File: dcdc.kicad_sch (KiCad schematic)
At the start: 25 parts, among them U2 LMR51450F

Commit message: Start layout
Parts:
- removed TP12: SW, meteopress_footprints:TestPoint_THTPad_D2.0mm_Drill1.0mm, symbol Connector:TestPoint
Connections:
- net V_{out}: now also R23.1
- net SW: now reaches C7.2, L1.1, U2.1 (SW), U2.2 (SW), U2.3 (SW)
- net SW: no longer R23.1
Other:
- moved on the sheet: JP2, L1, R23, R24

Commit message: Minor updates
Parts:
- removed C13, C14, C15, C16, C17, C18, C19: 10u, Capacitor_SMD:C_1206_3216Metric, symbol Device:C
- added C6: 100u (EEEFTH101XAP), Capacitor_SMD:CP_Elec_6.3x7.7, symbol Device:C_Polarized
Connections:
- net GND: now also C6.2
- net V_{out}: now also C6.1
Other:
- moved on the sheet: C10, C11, C12, C20, C7, C8, C9, D1, JP2, L1, R22, R23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

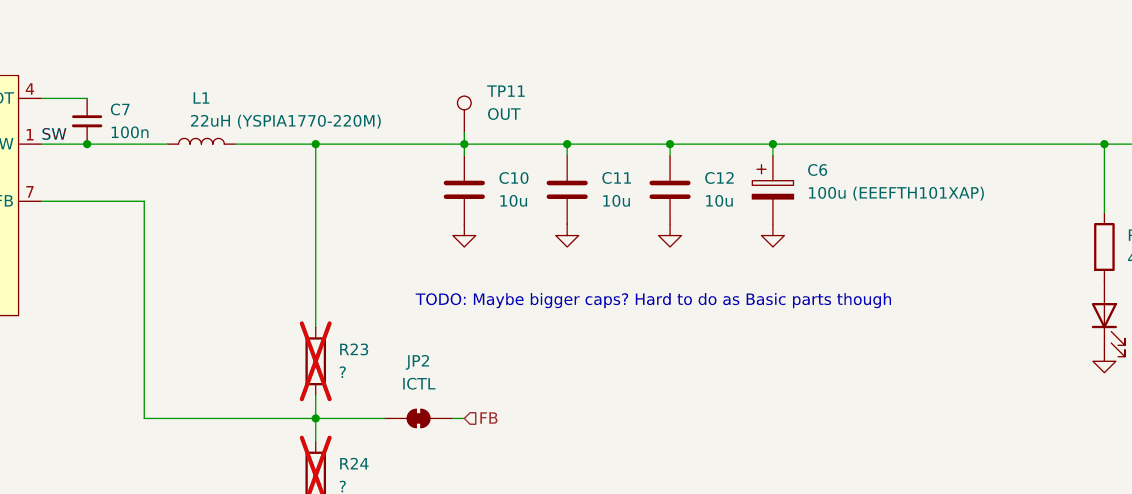
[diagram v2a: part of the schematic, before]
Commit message: Manufacturing update + inductor fix
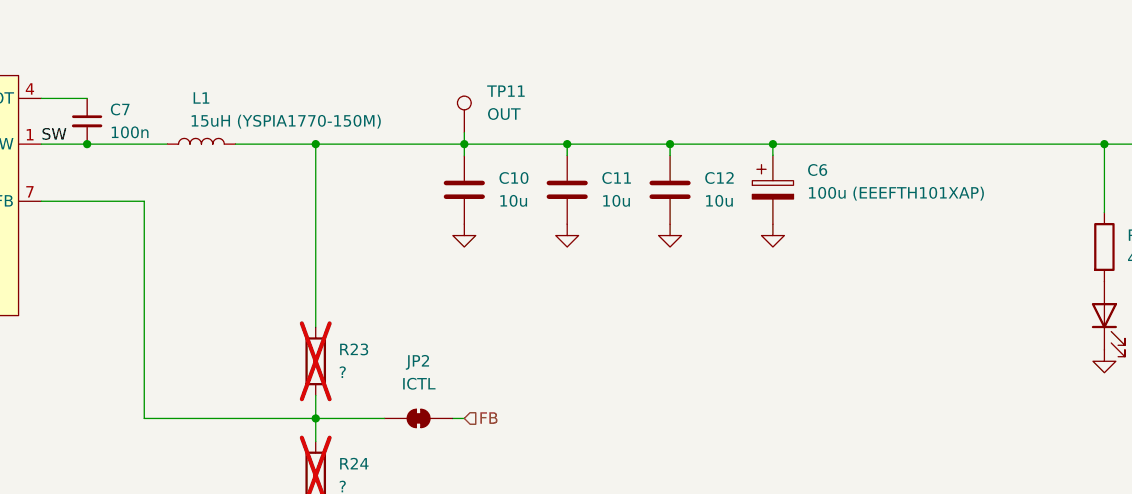
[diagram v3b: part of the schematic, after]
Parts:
- L1: value 22uH (YSPIA1770-220M) -> 15uH (YSPIA1770-150M); LCSC C2839932 -> C2839931
- TP11: LCSC C5199804 -> (none)
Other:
- note removed: "TODO: Maybe bigger caps? Hard to do as Basic parts though"
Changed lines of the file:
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@@
 		)
 	)
-	(text "TODO: Maybe bigger caps? Hard to do as Basic parts though"
-		(exclude_from_sim no)
-		(at 196.342 102.616 0)
+	(label "SW"
+		(at 128.27 85.09 0)
+		(fields_autoplaced yes)
 		(effects
 			(font
 				(size 1.27 1.27)
 			)
-		)
-	)
-	(label "SW"
-		(at 128.27 85.09 0)
+			(justify left bottom)
+		)
+	)
+	(hierarchical_label "EN"
+		(shape input)
+		(at 90.17 90.17 180)
 		(fields_autoplaced yes)
 		(effects
@@
 				(size 1.27 1.27)
 			)
-			(justify left bottom)
-		)
-	)
-	(hierarchical_label "EN"
+			(justify right)
+		)
+	)
+	(hierarchical_label "FB"
 		(shape input)
-		(at 90.17 90.17 180)
+		(at 175.26 115.57 0)
 		(fields_autoplaced yes)
 		(effects
@@
 				(size 1.27 1.27)
 			)
-			(justify right)
-		)
-	)
-	(hierarchical_label "FB"
-		(shape input)
-		(at 175.26 115.57 0)
+			(justify left)
+		)
+	)
+	(hierarchical_label "V_{out}"
+		(shape output)
+		(at 259.08 85.09 0)
 		(fields_autoplaced yes)
 		(effects
@@
 		)
 	)
-	(hierarchical_label "V_{out}"
-		(shape output)
-		(at 259.08 85.09 0)
+	(hierarchical_label "V_{in}"
+		(shape input)
+		(at 50.8 85.09 180)
 		(fields_autoplaced yes)
 		(effects
@@
 				(size 1.27 1.27)
 			)
-			(justify left)
-		)
-	)
-	(hierarchical_label "V_{in}"
-		(shape input)
-		(at 50.8 85.09 180)
-		(fields_autoplaced yes)
-		(effects
-			(font
-				(size 1.27 1.27)
-			)
 			(justify right)
 		)
@@
 			)
 		)
-		(property "Value" "22uH (YSPIA1770-220M)"
+		(property "Value" "15uH (YSPIA1770-150M)"
 			(at 155.448 82.55 90)
 			(effects
@@
 			)
 		)
-		(property "LCSC" "C2839932"
+		(property "LCSC" "C2839931"
 			(at 146.05 85.09 90)
 			(effects
@@
 			(at 175.26 83.82 0)
 			(effects
-				(font
-					(size 1.27 1.27)
-				)
-				(hide yes)
-			)
-		)
-		(property "LCSC" "C5199804"
-			(at 175.26 83.82 0)
-			(effects
